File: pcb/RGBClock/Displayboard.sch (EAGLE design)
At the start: 19 parts, among them IC1 MCP23017SO, U1 P82B96DR, U2 TPS71533DCKR, U4 P82B96DR, U5 PCA9685PW, U6 ZXLD1362ET5TA, X1 5566-4, X2 5566-2

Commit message: updating displayboard
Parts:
- removed U1: P82B96DR, Texas:P82B96DR
- added D5, D6: CDSOD323-T03C, MyComponents:CDSOD323-T03C
- added U3: LP3878MR-ADJ, Texas:LP3878MR-ADJ
- added U7: P82B96DR, Texas:P82B96DR
- added X3: 1503_09, con-lumberg:1503_09
- added X4, X5: (no value), con-molex-micro-fit-3_0:HEADER_POS4_43045-0401
- added X6: (no value), con-molex-micro-fit-3_0:HEADER_POS2_43045-0200
- X2: value 5566-2 -> (none); device con-molex:5566-2 -> con-molex-micro-fit-3_0:HEADER_POS2_43045-0200
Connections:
- removed net N$12: R5.1, U4.SY, U5.SCL
- removed net N$17: D1.KAT, U4.RX, U4.TX, X1-2.S
- new net +3V3: U2.OUT, U7.VCC, X4.1, X5.1
- new net D1: CON1.1, IC1.GPA0
- new net D2: CON1.2, IC1.GPA1
- new net D3: CON1.3, IC1.GPA2
- new net D4: CON1.4, IC1.GPA3
- new net D5: CON1.5, IC1.GPA4
- new net D6: CON1.6, IC1.GPA5
- new net D7: CON1.7, IC1.GPA6
- new net D8: CON1.8, IC1.GPA7
- new net N$2: D1.KAT, U4.RX, U4.TX, U7.RX, U7.TX, X1-2.S
- new net N$36: D6.P$2, U$1.RIN
- new net N$37: D5.P$2, U$1.LIN
- new net N$4: CON1.10, IC1.GPB0
- new net N$47: X3.2
- new net N$49: X3.3
- new net N$5: CON1.9, IC1.GPB1
- new net N$7: CON1.11, IC1.GPB2
- new net N$9: U7.SY, X4.3, X5.3
- new net SCL: CON1.12, IC1.SCL, R5.1, U$1.SCL, U4.SY, U5.SCL
- new net SDA: CON1.14, IC1.SDA, R7.1, U$1.SDA, U4.SX, U5.SDA
- net +5V: now also CON1.15
- net GND: now also CON1.13, D5.P$1, D6.P$1, U7.GND, X3.1, X4.4, X5.4
- net N$22: now also U7.RY, U7.TY
- net N$3: now also U7.SX, X4.2; no longer R7.1, U4.SX, U5.SDA
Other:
- moved on the sheet: CON1, D1, D2, U2, U4, X1-1, X1-2, X1-3, X1-4

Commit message: Mainboard, Displayboard, Leddriverboard
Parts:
- removed D10: HSMS-2800-TR1G, diode:BAS70
- removed D6: CDSOD323-T03C, MyComponents:CDSOD323-T03C
- removed JP1: (no value), jumper:JP1E
- removed U7: P82B96DR, Texas:P82B96DR
- added C1: 4u7, rcl:C-EUC1206
- added C10, C11, C16, C6, C8, C9: 0.47u, rcl:C-EUC0805
- added C12, C14, C5: 100n, rcl:C-EUC0805
- added C13: 2.2uF, AVX_By_element14_Batch_1:08053C225KAT2A
- added C15: 10u, rcl:C-EUC2012
- added C2: 10n, rcl:C-EUC1608
- added C3: 680p, rcl:C-EUC1608
- added C7: 0,47u, rcl:C-EUC1206
- added D3: SMA6F, MyComponents:SMA6F
- added D4: CDSOD323-T03C, MyComponents:CDSOD323-T03C
- added R1: 4.02k, resistor:R-EU_R0603
- added R10, R16, R17, R20: A1-1, resistor:R-EU_R0402
- added R11, R22, R6: A1-0, resistor:R-EU_R0402
- added R12, R14, R18: A0-1, resistor:R-EU_R0402
- added R13, R15, R19: A0-0, resistor:R-EU_R0402
- added R2: 1k, resistor:R-EU_R0603
- added R21: A2-1, resistor:R-EU_R0402
- added R23: A2-0, resistor:R-EU_R0402
- added R3, R4: 3300, rcl:R-EU_0204/7
- added R9: 0.833R, resistor:R-EU_R0603
- added U1: LP3878MR-ADJ, Texas:LP3878MR-ADJ
- C4: value 2.2uF -> 10u; device AVX_By_element14_Batch_1:08053C225KAT2A -> rcl:C-EUC2012
- CON1: device con-harting:CON20 -> con-harting:CON16
- D1: value SMA6F -> MUR480ERLG; device MyComponents:SMA6F -> diode:MUR150RL
- D5: value CDSOD323-T03C -> VS-30BQ100PBF; device MyComponents:CDSOD323-T03C -> MyComponents:VS-30BQ100PBF
- R5: value 3300 -> A1-1; device rcl:R-EU_0204/7 -> resistor:R-EU_R0402
- R7: value 3300 -> A0-1; device rcl:R-EU_0204/7 -> resistor:R-EU_R0402
- R8: value 0.3R -> A0-0; device resistor:R-EU_R0603 -> resistor:R-EU_R0402
- U2: value TPS71533DCKR -> P82B96DR; device Texas:TPS71533DCKR -> Texas:P82B96DR
- U3: value LP3878MR-ADJ -> P82B96DR; device Texas:LP3878MR-ADJ -> Texas:P82B96DR
- U4: value P82B96DR -> PCA9685PW; device Texas:P82B96DR -> NXP_By_element14_Batch_1:PCA9685PW
- U5: value PCA9685PW -> TPS71533DCKR; device NXP_By_element14_Batch_1:PCA9685PW -> Texas:TPS71533DCKR
- X2: device con-molex-micro-fit-3_0:HEADER_POS2_43045-0200 -> con-molex-micro-fit-3_0:HEADER_POS4_43045-0401
- X3: value 1503_09 -> (none); device con-lumberg:1503_09 -> con-molex-micro-fit-3_0:HEADER_POS4_43045-0401
- X4: value (none) -> 1503_09; device con-molex-micro-fit-3_0:HEADER_POS4_43045-0401 -> con-lumberg:1503_09
- X5: device con-molex-micro-fit-3_0:HEADER_POS4_43045-0401 -> con-molex-micro-fit-3_0:HEADER_POS2_43045-0200
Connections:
- removed net N$36: D6.P$2, U$1.RIN
- removed net N$37: D5.P$2, U$1.LIN
- removed net N$47: X3.2
- new net N$11: U$1.LOUT-, X5.2
- new net N$12: U$1.LOUT+, X5.1
- new net N$13: C6.2, U$1.LLINE-IN
- new net N$14: C11.2, U$1.RIN
- new net N$15: C10.2, U$1.LHPIN
- new net N$16: C9.2, U$1.LIN
- new net N$17: C8.2, U$1.PC-BEEP
- new net N$18: IC1.A1, R12.1, R13.2
- new net N$19: IC1.A0, R10.1, R11.2
- new net N$20: R21.1, R23.2, U4.A2
- new net N$21: IC1.A2, R14.1, R15.2
- new net N$23: C16.2, U$1.BYPASS
- new net N$24: C3.2, R1.2, R2.1, U1.ADJ
- new net N$25: D1.A, X1-4.S
- new net N$26: C2.1, U1.BYPASS
- new net N$27: CON1.16, R17.1
- new net N$28: CON1.15, R16.1
- new net N$29: R20.1, R22.2, U4.A1
- new net N$41: R7.1, R8.2, U$1.ADDRESS0
- new net N$42: R5.1, R6.2, U$1.ADDRESS1
- new net N$43: R18.1, R19.2, U4.A0
- net +3V3: now also C7.1, U3.VCC, U5.OUT, X2.1, X3.1; no longer U2.OUT, U7.VCC, X4.1, X5.1
- net +5V: now also C12.1, C14.1, C15.1, C3.1, C4.1, C5.1, CON1.2, IC1.VDD, R1.1, R10.2, R12.2, R14.2, R18.2, R20.2, R21.2, R3.2, R4.2, U$1.!SHUTDOWN, U$1.I2CVDD, U$1.PVDD1, U$1.PVDD2, U$1.VDD, U1.OUT, U2.VCC, U4.VDD, U5.IN; no longer CON1.15, U4.VCC, U5.VDD
- net D1: now also CON1.7; no longer CON1.1
- net D2: now also CON1.8; no longer CON1.2
- net D3: now also CON1.9; no longer CON1.3
- net D4: now also CON1.10; no longer CON1.4
- net D5: now also CON1.11; no longer CON1.5
- net D6: now also CON1.12; no longer CON1.6
- net D7: now also CON1.13; no longer CON1.7
- net D8: now also CON1.14; no longer CON1.8
- net GND: now also C1.2, C10.1, C11.1, C12.2, C13.C1, C14.2, C15.2, C16.1, C2.2, C4.2, C5.2, C7.2, C8.1, C9.1, CON1.1, D3.AN, D4.P$1, IC1.VSS, R11.1, R13.1, R15.1, R19.1, R2.2, R22.1, R23.1, R6.1, R8.1, U$1.GND1, U$1.GND2, U$1.HEATSINK, U$1.RHPIN, U$1.RLINE-IN, U$1.SE/!BTL, U1.GND, U1.GND_2, U2.GND, U3.GND, U4.A3, U4.A4, U4.A5, U4.EXTCLK, U4.VSS, U4.~OE, U5.GND, X1-3.S, X2.4, X3.4, X4.1; no longer C4.C1, CON1.13, D1.AN, D5.P$1, D6.P$1, U4.GND, U5.A0, U5.A1, U5.A2, U5.A3, U5.A4, U5.A5, U5.EXTCLK, U5.VSS, U5.~OE, U7.GND, X3.1, X4.4, X5.4
- net N$1: now also R9.1, X6.1; no longer JP1.1, R8.1
- net N$10: now also D5.A; no longer D10.A
- net N$2: now also D3.KAT, U2.RX, U2.TX, U3.RX, U3.TX; no longer D1.KAT, U4.RX, U4.TX, U7.RX, U7.TX
- net N$22: now also U2.RY, U2.TY, U3.RY, U3.TY; no longer U4.RY, U4.TY, U7.RY, U7.TY
- net N$3: now also U3.SX, X2.2, X3.2; no longer U7.SX, X4.2
- net N$4: now also CON1.5, IC1.GPB1; no longer CON1.10, IC1.GPB0
- net N$49: now also C6.1, D4.P$2, X4.3; no longer X3.3
- net N$5: now also CON1.4, IC1.GPB0; no longer CON1.9, IC1.GPB1
- net N$6: now also X6.2; no longer JP1.2
- net N$7: now also CON1.6; no longer CON1.11
- net N$8: now also U4.LED0; no longer U5.LED0
- net N$9: now also U3.SY, X2.3, X3.3; no longer U7.SY, X4.3, X5.3
- net SCL: now also R16.2, R3.1, U2.SY, U4.SCL; no longer CON1.12, R5.1, U4.SY, U5.SCL
- net SDA: now also R17.2, R4.1, U2.SX, U4.SDA; no longer CON1.14, R7.1, U4.SX, U5.SDA
- net VCC: now also C1.1, C13.C2, D1.C, D5.C, R9.2, U1.IN, U1.~SD; no longer C4.C2, D10.C, R8.2
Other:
- moved on the sheet: IC1, R5, R7, R8, U$1, X6

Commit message: 
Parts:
- removed X1: 5566-4, con-molex:5566-4
- added C17, C18: 0.47u, rcl:C-EUC0805
- added X7: (no value), con-molex-micro-fit-3_0:HEADER_POS4_43045-0401
- R10: value A1-1 -> A0-1
- R11: value A1-0 -> A0-0
- R12: value A0-1 -> A1-1
- R13: value A0-0 -> A1-0
- R14: value A0-1 -> A2-1
- R15: value A0-0 -> A2-0
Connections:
- net N$4 renamed RW
- net N$5 renamed RS
- net N$7 renamed E
- removed net D8: CON1.14, IC1.GPA7
- new net D0: CON1.7, IC1.GPA0
- new net N$4: C18.1, U$1.RHPIN
- new net N$5: C17.1, U$1.RLINE-IN
- net D1: now also CON1.8, IC1.GPA1; no longer CON1.7, IC1.GPA0
- net D2: now also CON1.9, IC1.GPA2; no longer CON1.8, IC1.GPA1
- net D3: now also CON1.10, IC1.GPA3; no longer CON1.9, IC1.GPA2
- net D4: now also CON1.11, IC1.GPA4; no longer CON1.10, IC1.GPA3
- net D5: now also CON1.12, IC1.GPA5; no longer CON1.11, IC1.GPA4
- net D6: now also CON1.13, IC1.GPA6; no longer CON1.12, IC1.GPA5
- net D7: now also CON1.14, IC1.GPA7; no longer CON1.13, IC1.GPA6
- net GND: now also C17.2, C18.2, X7.1; no longer U$1.RHPIN, U$1.RLINE-IN, X1-3.S
- net N$2: now also X7.3; no longer X1-2.S
- net N$22: now also X7.2; no longer X1-1.S
- net N$25: now also X7.4; no longer X1-4.S
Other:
- moved on the sheet: C1, C16, C5, C7, D2, D3

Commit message: 
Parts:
- added C19: 22n, rcl:C-EUC0805
- added R24: 3300, rcl:R-EU_0204/7
- added U7: 74HCT1G14GW, NXP_By_element14_Batch_1:74HCT1G14GW
- added U8: 74HCT1G86GW, NXP_By_element14_Batch_1:74HCT1G86GW
- X2, X3, X7: value (none) -> 43045-0400
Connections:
- removed net E: CON1.6, IC1.GPB2
- new net N$3: IC1.GPB2, R24.2, U8.A
- new net N$30: C19.2, R24.1, U7.A
- new net N$31: U7.Y, U8.B
- new net N$32: CON1.6, U8.Y
- net +5V: now also IC1.!RESET, U7.VCC, U8.VCC
- net GND: now also C19.1, U7.GND, U8.GND
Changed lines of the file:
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@@
 <part name="P+4" library="supply1" deviceset="+5V" device=""/>
 <part name="GND5" library="supply1" deviceset="GND" device=""/>
-<part name="X2" library="con-molex-micro-fit-3_0" deviceset="HEADER_POS4_?" device="43045-0401"/>
-<part name="X3" library="con-molex-micro-fit-3_0" deviceset="HEADER_POS4_?" device="43045-0401"/>
+<part name="X2" library="con-molex-micro-fit-3_0" deviceset="HEADER_POS4_?" device="43045-0401" value="43045-0400"/>
+<part name="X3" library="con-molex-micro-fit-3_0" deviceset="HEADER_POS4_?" device="43045-0401" value="43045-0400"/>
 <part name="X5" library="con-molex-micro-fit-3_0" deviceset="HEADER_POS2_?" device="43045-0200"/>
 <part name="X6" library="con-molex-micro-fit-3_0" deviceset="HEADER_POS2_?" device="43045-0200"/>
@@
 <part name="C17" library="rcl" deviceset="C-EU" device="C0805" value="0.47u"/>
 <part name="C18" library="rcl" deviceset="C-EU" device="C0805" value="0.47u"/>
-<part name="X7" library="con-molex-micro-fit-3_0" deviceset="HEADER_POS4_?" device="43045-0401"/>
+<part name="X7" library="con-molex-micro-fit-3_0" deviceset="HEADER_POS4_?" device="43045-0401" value="43045-0400"/>
+<part name="U7" library="NXP_By_element14_Batch_1" deviceset="74HCT1G14GW" device=""/>
+<part name="U8" library="NXP_By_element14_Batch_1" deviceset="74HCT1G86GW" device=""/>
+<part name="P+16" library="supply1" deviceset="+5V" device=""/>
+<part name="P+17" library="supply1" deviceset="+5V" device=""/>
+<part name="GND25" library="supply1" deviceset="GND" device=""/>
+<part name="GND26" library="supply1" deviceset="GND" device=""/>
+<part name="R24" library="rcl" deviceset="R-EU_" device="0204/7" value="3300"/>
+<part name="C19" library="rcl" deviceset="C-EU" device="C0805" value="22n"/>
+<part name="GND27" library="supply1" deviceset="GND" device=""/>
 </parts>
 <sheets>
@@
 <instance part="C18" gate="G$1" x="238.76" y="-73.66"/>
 <instance part="X7" gate="G$1" x="-27.94" y="66.04" rot="R180"/>
+<instance part="U7" gate="A" x="373.38" y="-86.36"/>
+<instance part="U8" gate="A" x="424.18" y="-60.96"/>
+<instance part="P+16" gate="1" x="353.06" y="-76.2"/>
+<instance part="P+17" gate="1" x="403.86" y="-50.8"/>
+<instance part="GND25" gate="1" x="353.06" y="-101.6"/>
+<instance part="GND26" gate="1" x="403.86" y="-76.2"/>
+<instance part="R24" gate="G$1" x="335.28" y="-86.36" rot="R180"/>
+<instance part="C19" gate="G$1" x="342.9" y="-96.52" smashed="yes" rot="R180">
+<attribute name="NAME" x="348.996" y="-96.901" size="1.778" layer="95" rot="R180"/>
+<attribute name="VALUE" x="351.536" y="-91.821" size="1.778" layer="96" rot="R180"/>
+</instance>
+<instance part="GND27" gate="1" x="342.9" y="-101.6"/>
 </instances>
 <busses>
-<bus name="D[0..7],RS,RW,E">
+<bus name="D[0..7],RS,RW">
 <segment>
 <wire x1="358.14" y1="-25.4" x2="358.14" y2="7.62" width="0.762" layer="92"/>
@@
 <pinref part="X7" gate="G$1" pin="1"/>
 </segment>
+<segment>
+<pinref part="U7" gate="A" pin="GND"/>
+<pinref part="GND25" gate="1" pin="GND"/>
+<wire x1="355.6" y1="-96.52" x2="353.06" y2="-96.52" width="0.1524" layer="91"/>
+<wire x1="353.06" y1="-96.52" x2="353.06" y2="-99.06" width="0.1524" layer="91"/>
+</segment>
+<segment>
+<pinref part="U8" gate="A" pin="GND"/>
+<pinref part="GND26" gate="1" pin="GND"/>
+<wire x1="406.4" y1="-71.12" x2="403.86" y2="-71.12" width="0.1524" layer="91"/>
+<wire x1="403.86" y1="-71.12" x2="403.86" y2="-73.66" width="0.1524" layer="91"/>
+</segment>
+<segment>
+<pinref part="C19" gate="G$1" pin="1"/>
+<pinref part="GND27" gate="1" pin="GND"/>
+</segment>
 </net>
 <net name="VCC" class="2">
@@
 <pinref part="IC1" gate="G$1" pin="VDD"/>
 <wire x1="317.5" y1="7.62" x2="325.12" y2="7.62" width="0.1524" layer="91"/>
+<pinref part="IC1" gate="G$1" pin="!RESET"/>
+<wire x1="325.12" y1="2.54" x2="317.5" y2="2.54" width="0.1524" layer="91"/>
+<wire x1="317.5" y1="2.54" x2="317.5" y2="7.62" width="0.1524" layer="91"/>
+<junction x="317.5" y="7.62"/>
 </segment>
 <segment>
@@
 <junction x="248.92" y="-48.26"/>
 <junction x="248.92" y="-55.88"/>
+</segment>
+<segment>
+<pinref part="P+17" gate="1" pin="+5V"/>
+<wire x1="403.86" y1="-53.34" x2="403.86" y2="-58.42" width="0.1524" layer="91"/>
+<pinref part="U8" gate="A" pin="VCC"/>
+<wire x1="403.86" y1="-58.42" x2="406.4" y2="-58.42" width="0.1524" layer="91"/>
+</segment>
+<segment>
+<pinref part="P+16" gate="1" pin="+5V"/>
+<wire x1="353.06" y1="-78.74" x2="353.06" y2="-81.28" width="0.1524" layer="91"/>
+<pinref part="U7" gate="A" pin="VCC"/>
+<wire x1="353.06" y1="-81.28" x2="355.6" y2="-81.28" width="0.1524" layer="91"/>
 </segment>
 </net>
@@
 </segment>
 </net>
-<net name="E" class="0">
-<segment>
-<pinref part="IC1" gate="G$1" pin="GPB2"/>
-<wire x1="358.14" y1="-20.32" x2="350.52" y2="-20.32" width="0.1524" layer="91"/>
-<label x="360.68" y="-20.32" size="1.778" layer="95"/>
-</segment>
-<segment>
-<pinref part="CON1" gate="G$1" pin="6"/>
-<wire x1="381" y1="-2.54" x2="386.08" y2="-2.54" width="0.1524" layer="91"/>
-<label x="373.38" y="-2.54" size="1.778" layer="95"/>
-</segment>
-</net>
 <net name="N$4" class="0">
 <segment>
@@
 <net name="N$7" class="0">
 <segment>
-<pinref part="X3" gate="G$1" pin="2"/>
-<wire x1="114.3" y1="-119.38" x2="116.84" y2="-119.38" width="0.1524" layer="91"/>
 <pinref part="U3" gate="A" pin="SX"/>
 <wire x1="76.2" y1="0" x2="88.9" y2="0" width="0.1524" layer="91"/>
@@
 <wire x1="88.9" y1="-93.98" x2="114.3" y2="-93.98" width="0.1524" layer="91"/>
 <junction x="88.9" y="-93.98"/>
-<wire x1="114.3" y1="-119.38" x2="88.9" y2="-119.38" width="0.1524" layer="91"/>
+<pinref part="X3" gate="G$1" pin="2"/>
+<wire x1="88.9" y1="-119.38" x2="114.3" y2="-119.38" width="0.1524" layer="91"/>
+</segment>
+</net>
+<net name="N$3" class="0">
+<segment>
+<pinref part="IC1" gate="G$1" pin="GPB2"/>
+<wire x1="350.52" y1="-20.32" x2="355.6" y2="-20.32" width="0.1524" layer="91"/>
+<wire x1="355.6" y1="-20.32" x2="355.6" y2="-63.5" width="0.1524" layer="91"/>
+<wire x1="355.6" y1="-63.5" x2="320.04" y2="-63.5" width="0.1524" layer="91"/>
+<wire x1="320.04" y1="-63.5" x2="320.04" y2="-86.36" width="0.1524" layer="91"/>
+<pinref part="U8" gate="A" pin="A"/>
+<wire x1="355.6" y1="-63.5" x2="406.4" y2="-63.5" width="0.1524" layer="91"/>
+<junction x="355.6" y="-63.5"/>
+<pinref part="R24" gate="G$1" pin="2"/>
+<wire x1="320.04" y1="-86.36" x2="330.2" y2="-86.36" width="0.1524" layer="91"/>
+</segment>
+</net>
+<net name="N$30" class="0">
+<segment>
+<pinref part="U7" gate="A" pin="A"/>
+<wire x1="340.36" y1="-86.36" x2="342.9" y2="-86.36" width="0.1524" layer="91"/>
+<pinref part="R24" gate="G$1" pin="1"/>
+<pinref part="C19" gate="G$1" pin="2"/>
+<wire x1="342.9" y1="-86.36" x2="355.6" y2="-86.36" width="0.1524" layer="91"/>
+<wire x1="342.9" y1="-91.44" x2="342.9" y2="-86.36" width="0.1524" layer="91"/>
+<junction x="342.9" y="-86.36"/>
+</segment>
+</net>
+<net name="N$31" class="0">
+<segment>
+<pinref part="U7" gate="A" pin="Y"/>
+<wire x1="391.16" y1="-81.28" x2="393.7" y2="-81.28" width="0.1524" layer="91"/>
+<wire x1="393.7" y1="-81.28" x2="393.7" y2="-66.04" width="0.1524" layer="91"/>
+<pinref part="U8" gate="A" pin="B"/>
+<wire x1="393.7" y1="-66.04" x2="406.4" y2="-66.04" width="0.1524" layer="91"/>
+</segment>
+</net>
+<net name="N$32" class="0">
+<segment>
+<pinref part="U8" gate="A" pin="Y"/>
+<wire x1="441.96" y1="-58.42" x2="441.96" y2="-40.64" width="0.1524" layer="91"/>
+<wire x1="441.96" y1="-40.64" x2="375.92" y2="-40.64" width="0.1524" layer="91"/>
+<wire x1="375.92" y1="-40.64" x2="375.92" y2="-2.54" width="0.1524" layer="91"/>
+<pinref part="CON1" gate="G$1" pin="6"/>
+<wire x1="375.92" y1="-2.54" x2="386.08" y2="-2.54" width="0.1524" layer="91"/>
 </segment>
 </net>
@@
 </sheet>
 </sheets>
+<errors>
+</errors>
 </schematic>
 </drawing>

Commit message: Cleanup schematic
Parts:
- R10: value A0-1 -> A0-0
- R11: value A0-0 -> A1-1
- R12: value A1-1 -> A1-0
- R13: value A1-0 -> A0-1
- R14: value A2-1 -> A0-0
- R15: value A2-0 -> 0.833R; device resistor:R-EU_R0402 -> resistor:R-EU_R0603
- R16: value A1-1 -> A0-1
- R17: value A1-1 -> A0-0
- R18, R7: value A0-1 -> A1-1
- R19, R8: value A0-0 -> A1-0
- R20, R5: value A1-1 -> A2-1
- R21: value A2-1 -> A2-0
- R22: value A1-0 -> 3300; device resistor:R-EU_R0402 -> rcl:R-EU_0204/7
- R23: value A2-0 -> A1-1
- R24: value 3300 -> A1-1; device rcl:R-EU_0204/7 -> resistor:R-EU_R0402
- R6: value A1-0 -> A2-0
- R9: value 0.833R -> A0-1; device resistor:R-EU_R0603 -> resistor:R-EU_R0402
- renumbered X7 to X1
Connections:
- net +5V: now also R11.2, R13.2, R16.2, R9.2; no longer R10.2, R12.2, R14.2, R21.2
- net GND: now also C16.2, C18.1, R10.1, R12.1, R14.1, R17.1, R21.1; no longer C16.1, C18.2, R11.1, R13.1, R15.1, R22.1, R23.1
- net N$1: now also R15.1; no longer R9.1
- net N$18: now also R18.1, R19.2; no longer R12.1, R13.2
- net N$19: now also R16.1, R17.2; no longer R10.1, R11.2
- net N$20: now also R5.1, R6.2; no longer R21.1, R23.2
- net N$21: now also R20.1, R21.2; no longer R14.1, R15.2
- net N$23: now also C18.2; no longer C16.2
- net N$27: now also R24.1; no longer R17.1
- net N$28: now also R23.1; no longer R16.1
- net N$29: now also R7.1, R8.2; no longer R20.1, R22.2
- net N$3: now also R22.2; no longer R24.2
- net N$30: now also R22.1; no longer R24.1
- net N$4: now also C16.1; no longer C18.1
- net N$41: now also R13.1, R14.2; no longer R7.1, R8.2
- net N$42: now also R11.1, R12.2; no longer R5.1, R6.2
- net N$43: now also R10.2, R9.1; no longer R18.1, R19.2
- net SCL: now also R23.2; no longer R16.2
- net SDA: now also R24.2; no longer R17.2
- net VCC: now also R15.2; no longer R9.2
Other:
- moved on the sheet: C16, C18, C3

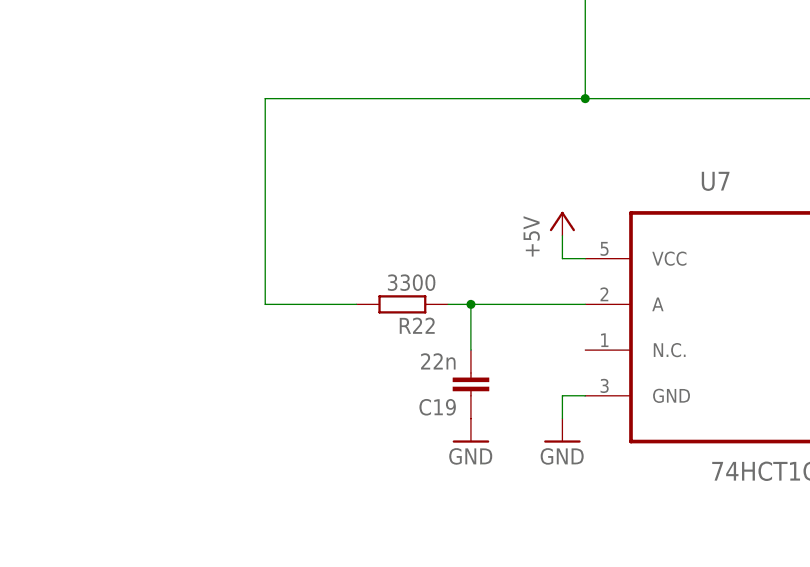
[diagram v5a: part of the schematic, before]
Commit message: 
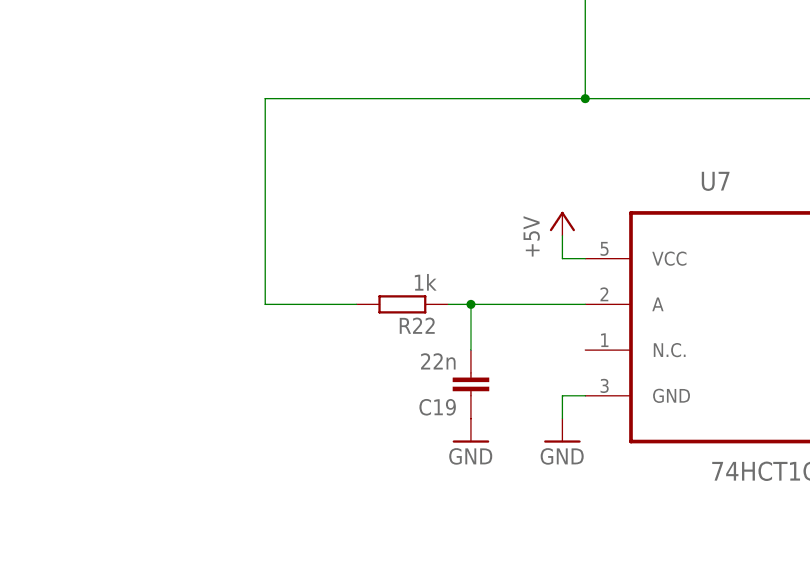
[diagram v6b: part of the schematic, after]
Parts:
- R22: value 3300 -> 1k
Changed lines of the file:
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@@
 <part name="GND25" library="supply1" deviceset="GND" device=""/>
 <part name="GND26" library="supply1" deviceset="GND" device=""/>
-<part name="R22" library="rcl" deviceset="R-EU_" device="0204/7" value="3300"/>
+<part name="R22" library="rcl" deviceset="R-EU_" device="0204/7" value="1k"/>
 <part name="C19" library="rcl" deviceset="C-EU" device="C0805" value="22n"/>
 <part name="GND27" library="supply1" deviceset="GND" device=""/>

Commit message: Routing displayoard and cleanup board
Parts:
- R23: value A1-1 -> SCL
- R24: value A1-1 -> SDA
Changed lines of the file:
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@@
 <part name="GND22" library="supply1" deviceset="GND" device=""/>
 <part name="D1" library="diode" deviceset="MUR150RL" device="" value="MUR480ERLG"/>
-<part name="R24" library="resistor" deviceset="R-EU_" device="R0402" value="A1-1"/>
-<part name="R23" library="resistor" deviceset="R-EU_" device="R0402" value="A1-1"/>
+<part name="R24" library="resistor" deviceset="R-EU_" device="R0402" value="SDA"/>
+<part name="R23" library="resistor" deviceset="R-EU_" device="R0402" value="SCL"/>
 <part name="CON1" library="con-harting" deviceset="CON16" device=""/>
 <part name="P+12" library="supply1" deviceset="VCC" device=""/>
@@
 </segment>
 </net>
-<net name="+3V3" class="0">
+<net name="+3V3" class="1">
 <segment>
 <pinref part="+3V1" gate="G$1" pin="+3V3"/>
